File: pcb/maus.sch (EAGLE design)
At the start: 85 parts, among them IC1 AD712R, Q1 BSS123, Q2 BSS123, Q4 BSS123, Q5 BSS123, U1 ESP32-S2-WROOM, U2 CH340C, U3 CP2102, U4 LP3965EMP-3.3, U5 LSM9DS1TR

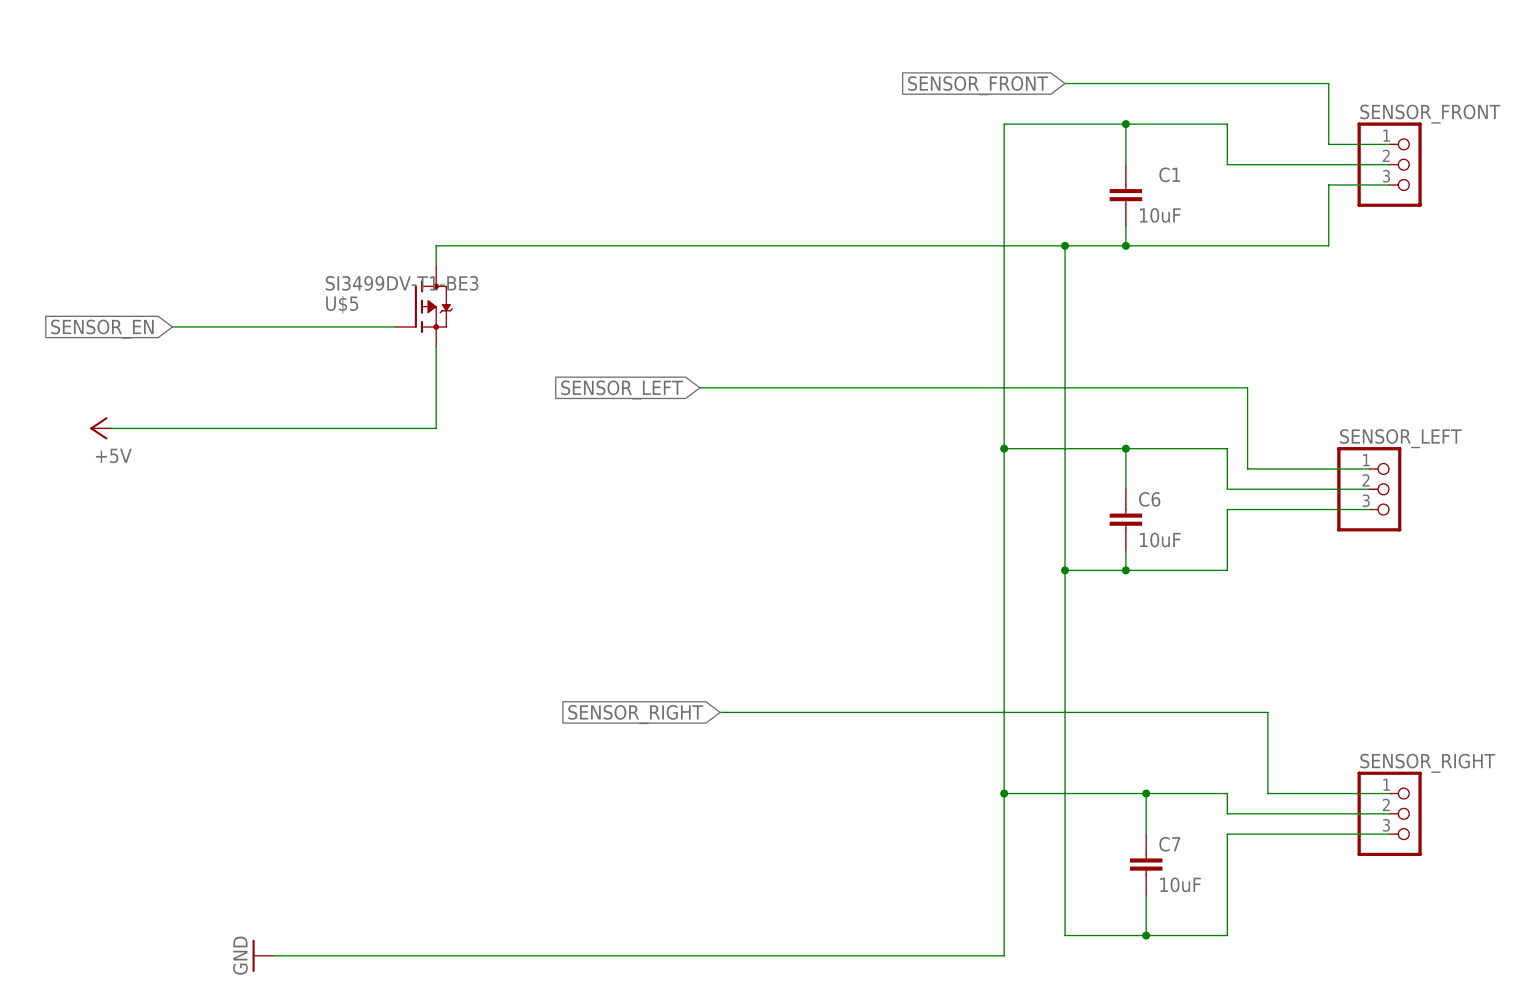
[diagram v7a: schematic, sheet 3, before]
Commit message: added driver for sensor power mosfet
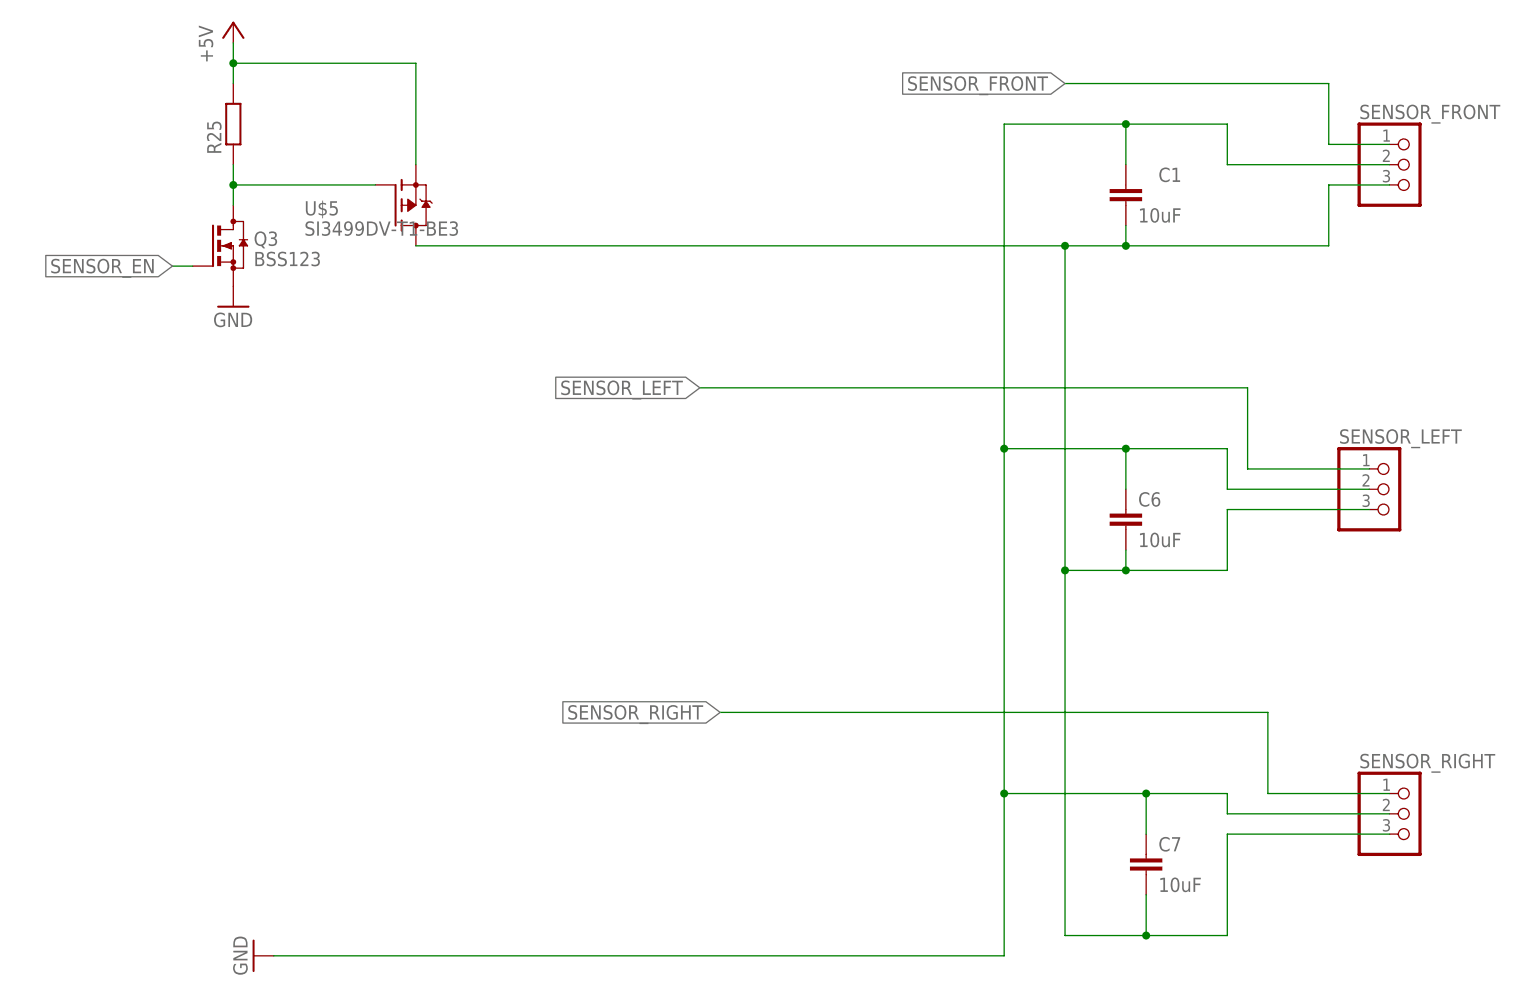
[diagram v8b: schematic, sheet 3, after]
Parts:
- added Q3: BSS123, transistor-small-signal:BSS123
- added R25: (no value), rcl:R-EU_R0805
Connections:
- new net N$2: Q3.D, R25.1, U$5.G
- net +5V: now also R25.2
- net GND: now also Q3.S
- net SENSOR_EN: now also Q3.G; no longer U$5.G
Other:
- moved on the sheet: U$5
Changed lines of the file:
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@@
 <part name="U$5" library="mosfet" deviceset="SI3499DV-T1-BE3" device="" package3d_urn="urn:adsk.eagle:package:33743404/1"/>
 <part name="U$6" library="mosfet" deviceset="SI3499DV-T1-BE3" device="" package3d_urn="urn:adsk.eagle:package:33743404/1"/>
+<part name="Q3" library="transistor-small-signal" library_urn="urn:adsk.eagle:library:401" deviceset="BSS123" device="" package3d_urn="urn:adsk.eagle:package:28738/2"/>
+<part name="R25" library="rcl" library_urn="urn:adsk.eagle:library:334" deviceset="R-EU_" device="R0805" package3d_urn="urn:adsk.eagle:package:23553/2"/>
+<part name="GND41" library="supply1" library_urn="urn:adsk.eagle:library:371" deviceset="GND" device=""/>
 </parts>
 <sheets>
@@
 <attribute name="VALUE" x="181.61" y="20.32" size="1.778" layer="96"/>
 </instance>
-<instance part="P+1" gate="1" x="22.86" y="76.2" smashed="yes" rot="R90">
-<attribute name="VALUE" x="27.94" y="73.66" size="1.778" layer="96" rot="R180"/>
-</instance>
-<instance part="U$5" gate="T$1" x="63.5" y="91.44" smashed="yes" rot="MR180">
-<attribute name="VALUE" x="52.07" y="95.25" size="1.778" layer="96" rot="MR180"/>
-<attribute name="NAME" x="52.07" y="92.71" size="1.778" layer="95" rot="MR180"/>
+<instance part="P+1" gate="1" x="40.64" y="127" smashed="yes">
+<attribute name="VALUE" x="38.1" y="121.92" size="1.778" layer="96" rot="R90"/>
+</instance>
+<instance part="U$5" gate="T$1" x="60.96" y="104.14" smashed="yes">
+<attribute name="VALUE" x="49.53" y="100.33" size="1.778" layer="96"/>
+<attribute name="NAME" x="49.53" y="102.87" size="1.778" layer="95"/>
+</instance>
+<instance part="Q3" gate="G$1" x="40.64" y="99.06" smashed="yes">
+<attribute name="NAME" x="43.18" y="99.06" size="1.778" layer="95"/>
+<attribute name="VALUE" x="43.18" y="96.52" size="1.778" layer="96"/>
+</instance>
+<instance part="R25" gate="G$1" x="40.64" y="114.3" smashed="yes" rot="R90">
+<attribute name="NAME" x="39.1414" y="110.49" size="1.778" layer="95" rot="R90"/>
+<attribute name="VALUE" x="43.942" y="110.49" size="1.778" layer="96" rot="R90"/>
+</instance>
+<instance part="GND41" gate="1" x="40.64" y="91.44" smashed="yes">
+<attribute name="VALUE" x="38.1" y="88.9" size="1.778" layer="96"/>
 </instance>
 </instances>
@@
 <junction x="144.78" y="58.42"/>
 <wire x1="152.4" y1="58.42" x2="144.78" y2="58.42" width="0.1524" layer="91"/>
-<wire x1="144.78" y1="99.06" x2="66.04" y2="99.06" width="0.1524" layer="91"/>
+<wire x1="144.78" y1="99.06" x2="63.5" y2="99.06" width="0.1524" layer="91"/>
 <junction x="144.78" y="99.06"/>
 <pinref part="C1" gate="G$1" pin="2"/>
@@
 <wire x1="165.1" y1="66.04" x2="182.88" y2="66.04" width="0.1524" layer="91"/>
 <pinref part="U$5" gate="T$1" pin="D"/>
-<wire x1="66.04" y1="96.52" x2="66.04" y2="99.06" width="0.1524" layer="91"/>
 </segment>
 </net>
@@
 <wire x1="165.1" y1="68.58" x2="182.88" y2="68.58" width="0.1524" layer="91"/>
 </segment>
+<segment>
+<pinref part="Q3" gate="G$1" pin="S"/>
+<pinref part="GND41" gate="1" pin="GND"/>
+</segment>
 </net>
 <net name="SENSOR_EN" class="0">
 <segment>
-<wire x1="60.96" y1="88.9" x2="33.02" y2="88.9" width="0.1524" layer="91"/>
-<label x="33.02" y="88.9" size="1.778" layer="95" rot="R180" xref="yes"/>
-<pinref part="U$5" gate="T$1" pin="G"/>
-</segment>
-</net>
-<net name="+5V" class="0">
-<segment>
-<wire x1="25.4" y1="76.2" x2="66.04" y2="76.2" width="0.1524" layer="91"/>
-<pinref part="P+1" gate="1" pin="+5V"/>
-<pinref part="U$5" gate="T$1" pin="S"/>
-<wire x1="66.04" y1="86.36" x2="66.04" y2="76.2" width="0.1524" layer="91"/>
+<label x="33.02" y="96.52" size="1.778" layer="95" rot="R180" xref="yes"/>
+<pinref part="Q3" gate="G$1" pin="G"/>
+<wire x1="33.02" y1="96.52" x2="35.56" y2="96.52" width="0.1524" layer="91"/>
 </segment>
 </net>
@@
 </segment>
 </net>
+<net name="+5V" class="0">
+<segment>
+<pinref part="P+1" gate="1" pin="+5V"/>
+<pinref part="R25" gate="G$1" pin="2"/>
+<wire x1="40.64" y1="124.46" x2="40.64" y2="121.92" width="0.1524" layer="91"/>
+<pinref part="U$5" gate="T$1" pin="S"/>
+<wire x1="40.64" y1="121.92" x2="40.64" y2="119.38" width="0.1524" layer="91"/>
+<wire x1="40.64" y1="121.92" x2="63.5" y2="121.92" width="0.1524" layer="91"/>
+<wire x1="63.5" y1="121.92" x2="63.5" y2="109.22" width="0.1524" layer="91"/>
+<junction x="40.64" y="121.92"/>
+</segment>
+</net>
+<net name="N$2" class="0">
+<segment>
+<pinref part="R25" gate="G$1" pin="1"/>
+<pinref part="Q3" gate="G$1" pin="D"/>
+<wire x1="40.64" y1="109.22" x2="40.64" y2="106.68" width="0.1524" layer="91"/>
+<pinref part="U$5" gate="T$1" pin="G"/>
+<wire x1="40.64" y1="106.68" x2="40.64" y2="104.14" width="0.1524" layer="91"/>
+<wire x1="40.64" y1="106.68" x2="58.42" y2="106.68" width="0.1524" layer="91"/>
+<junction x="40.64" y="106.68"/>
+</segment>
+</net>
